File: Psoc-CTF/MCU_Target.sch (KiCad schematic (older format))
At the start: 44 parts, among them IC1 CY8C4248LQI-BL583, J4 Conn_01x04, P1 Power, P2 Analog, P3 Digital, P4 Digital, P5 CONN_01X01, P6 CONN_01X01, P7 CONN_01X01, P8 CONN_01X01, U4 FM24C04B-GTR, Y1 24MHz, Y2 32.768Khz

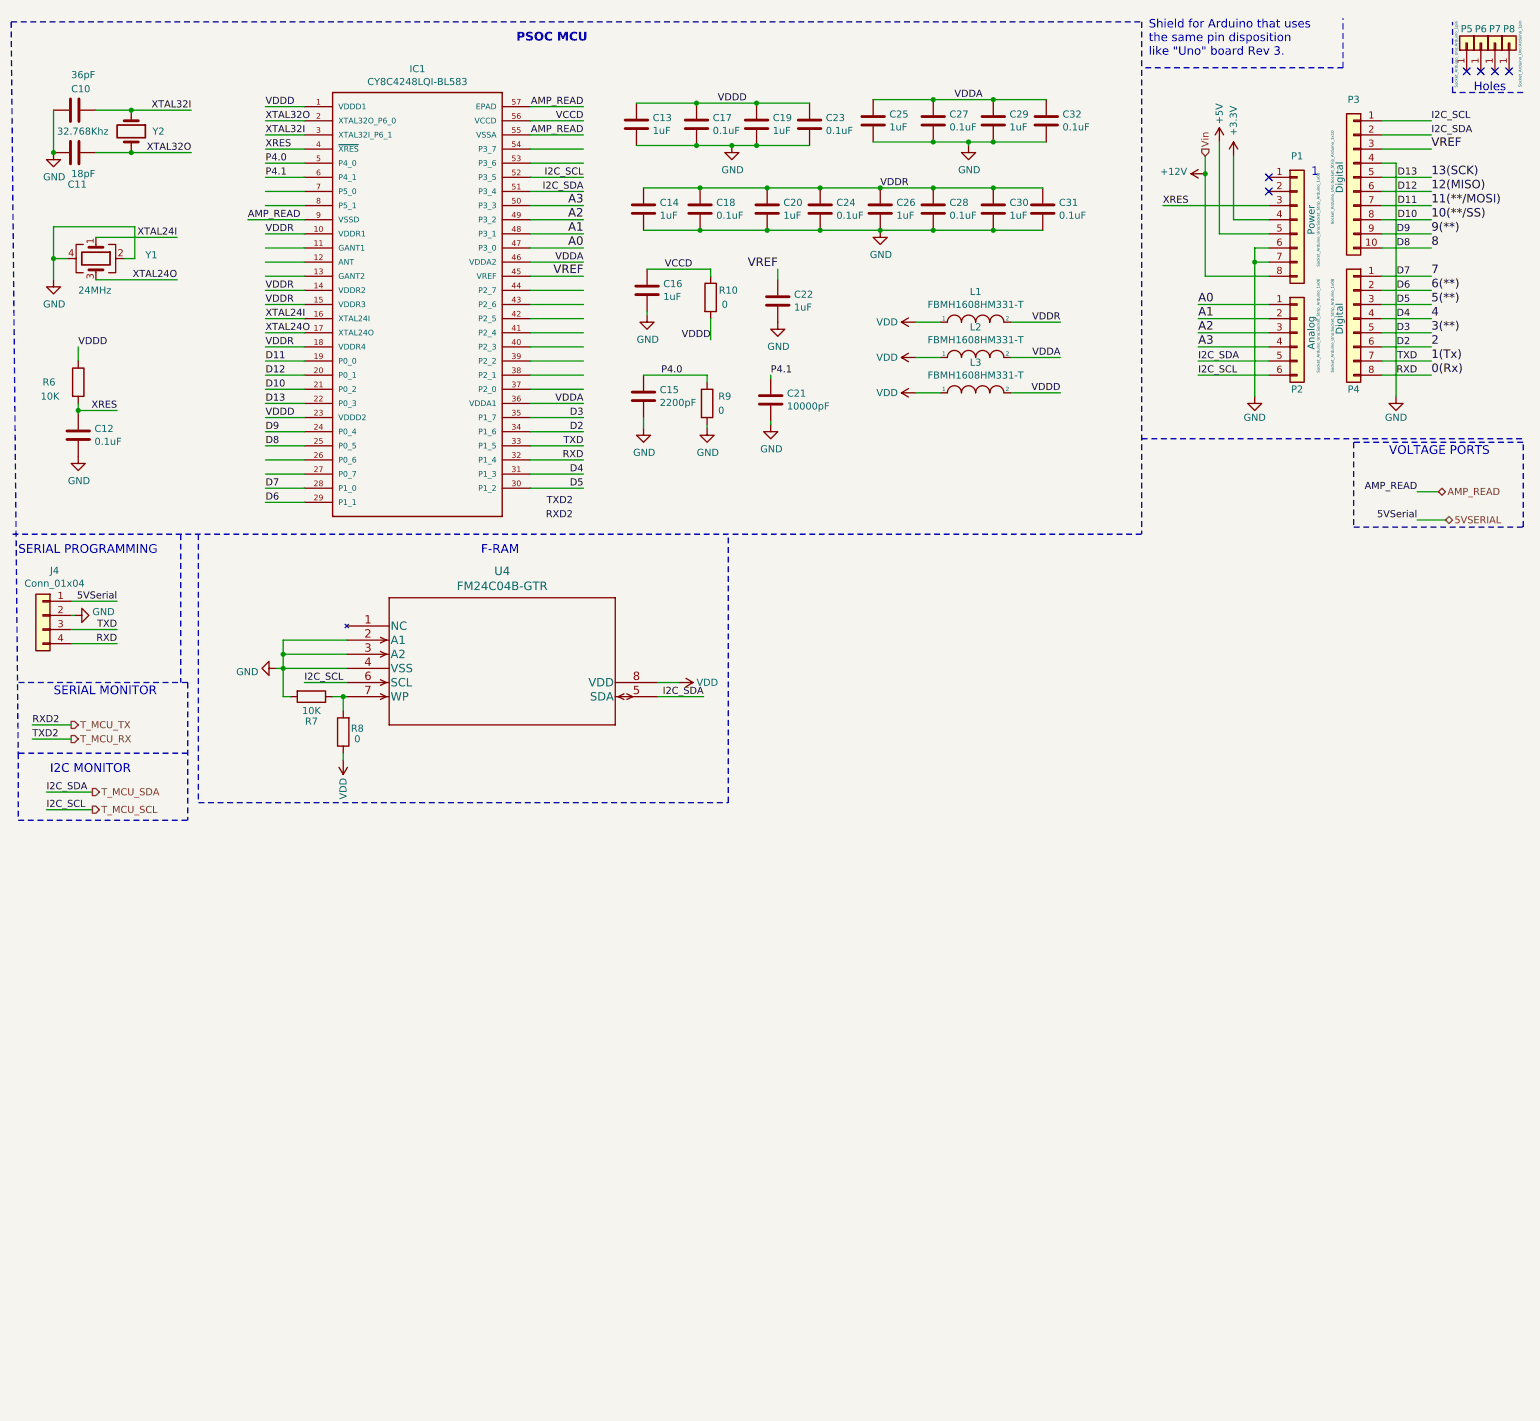
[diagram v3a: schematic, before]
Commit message: Antena agregada, pines de programación SWD
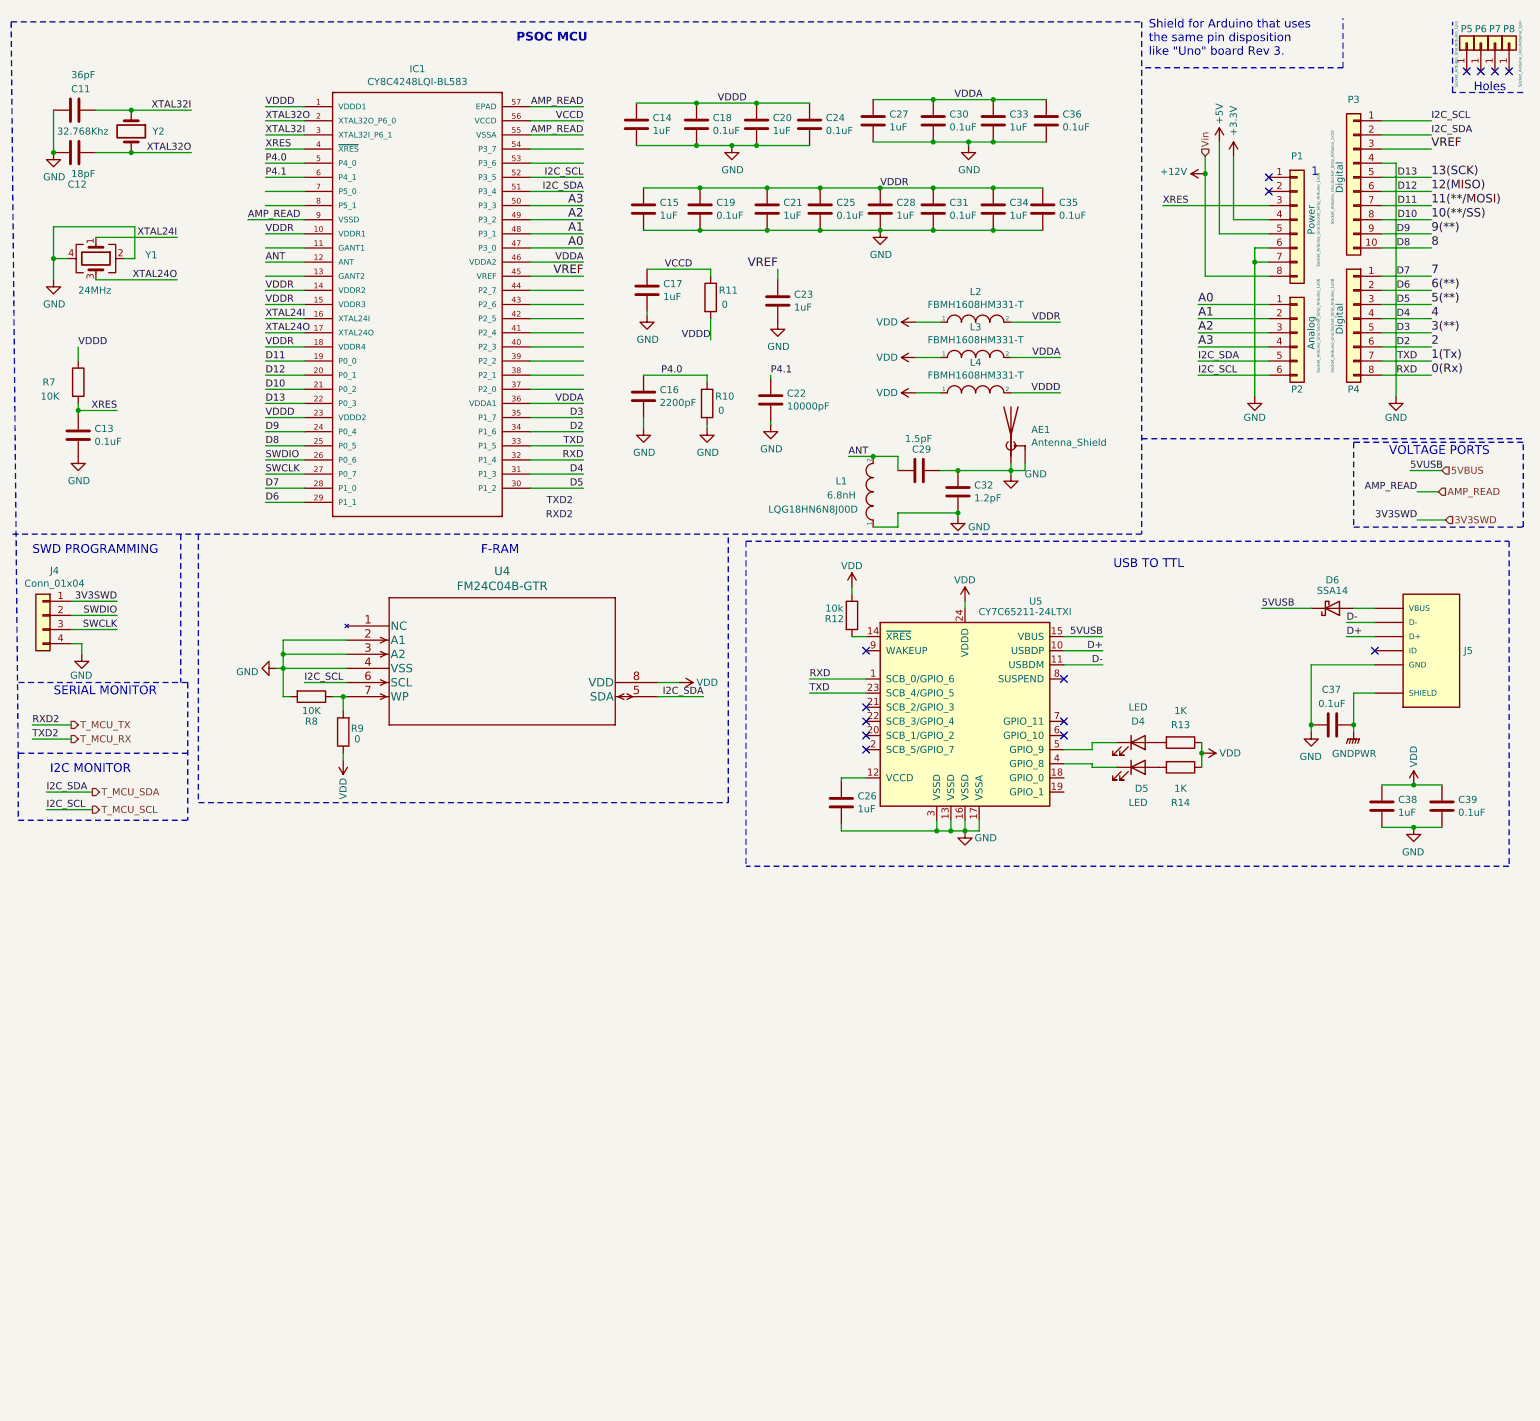
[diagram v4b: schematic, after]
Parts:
- added AE1: Antenna_Shield, symbol Device:Antenna_Shield
- added C26, C38: 1uF, Capacitor_SMD:C_0603_1608Metric_Pad1.08x0.95mm_HandSolder, symbol Device:C
- added C29: 1.5pF, Capacitor_SMD:C_0603_1608Metric_Pad1.08x0.95mm_HandSolder, symbol Device:C
- added C32: 1.2pF, Capacitor_SMD:C_0603_1608Metric_Pad1.08x0.95mm_HandSolder, symbol Device:C
- added C37, C39: 0.1uF, Capacitor_SMD:C_0603_1608Metric_Pad1.08x0.95mm_HandSolder, symbol Device:C
- added D4, D5: LED, LED_SMD:LED_0603_1608Metric_Pad1.05x0.95mm_HandSolder, symbol Device:LED
- added D6: SSA14, Diode_SMD:D_SMA_Handsoldering, symbol Device:D_Schottky
- added J5: USB3076-XX-X_REVC, Psoc-CTF:microUSB, symbol microUSB:USB3076-XX-X_REVC
- added L1: 6.8nH, Inductor_SMD:L_0603_1608Metric_Pad1.05x0.95mm_HandSolder, symbol pspice:INDUCTOR
- added R12: 10k, Resistor_SMD:R_0603_1608Metric_Pad0.98x0.95mm_HandSolder, symbol Device:R
- added R13, R14: 1K, Resistor_SMD:R_0603_1608Metric_Pad0.98x0.95mm_HandSolder, symbol Device:R
- added U5: CY7C65211-24LTXI, Package_DFN_QFN:QFN-24-1EP_4x4mm_P0.5mm_EP2.6x2.6mm, symbol Interface_USB:CY7C65211-24LTXI
- renumbered C10 to C11, C11 to C12, C12 to C13, C13 to C14, C14 to C15, C15 to C16, C16 to C17, C17 to C18, C18 to C19, C19 to C20, C20 to C21, C21 to C22, C22 to C23, C23 to C24, C24 to C25, C25 to C27, C26 to C28, C27 to C30, C28 to C31, C29 to C33, C30 to C34, C31 to C35, C32 to C36, L1 to L2, L2 to L3, L3 to L4, R9 to R10, R10 to R11, R6 to R7, R7 to R8, R8 to R9
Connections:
- net labels added: 3V3SWD, 5VBUS, 5VUSB, ANT, D+, D-, GNDPWR, SWCLK, SWDIO
- net labels removed: 5VSERIAL, 5VSerial
- wire segments 182 -> 238
- no-connect marks 6 -> 15
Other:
- note added: "SWD PROGRAMMING"
- note added: "USB TO TTL"
- note removed: "SERIAL PROGRAMMING"

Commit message: anexo slider y led rgb
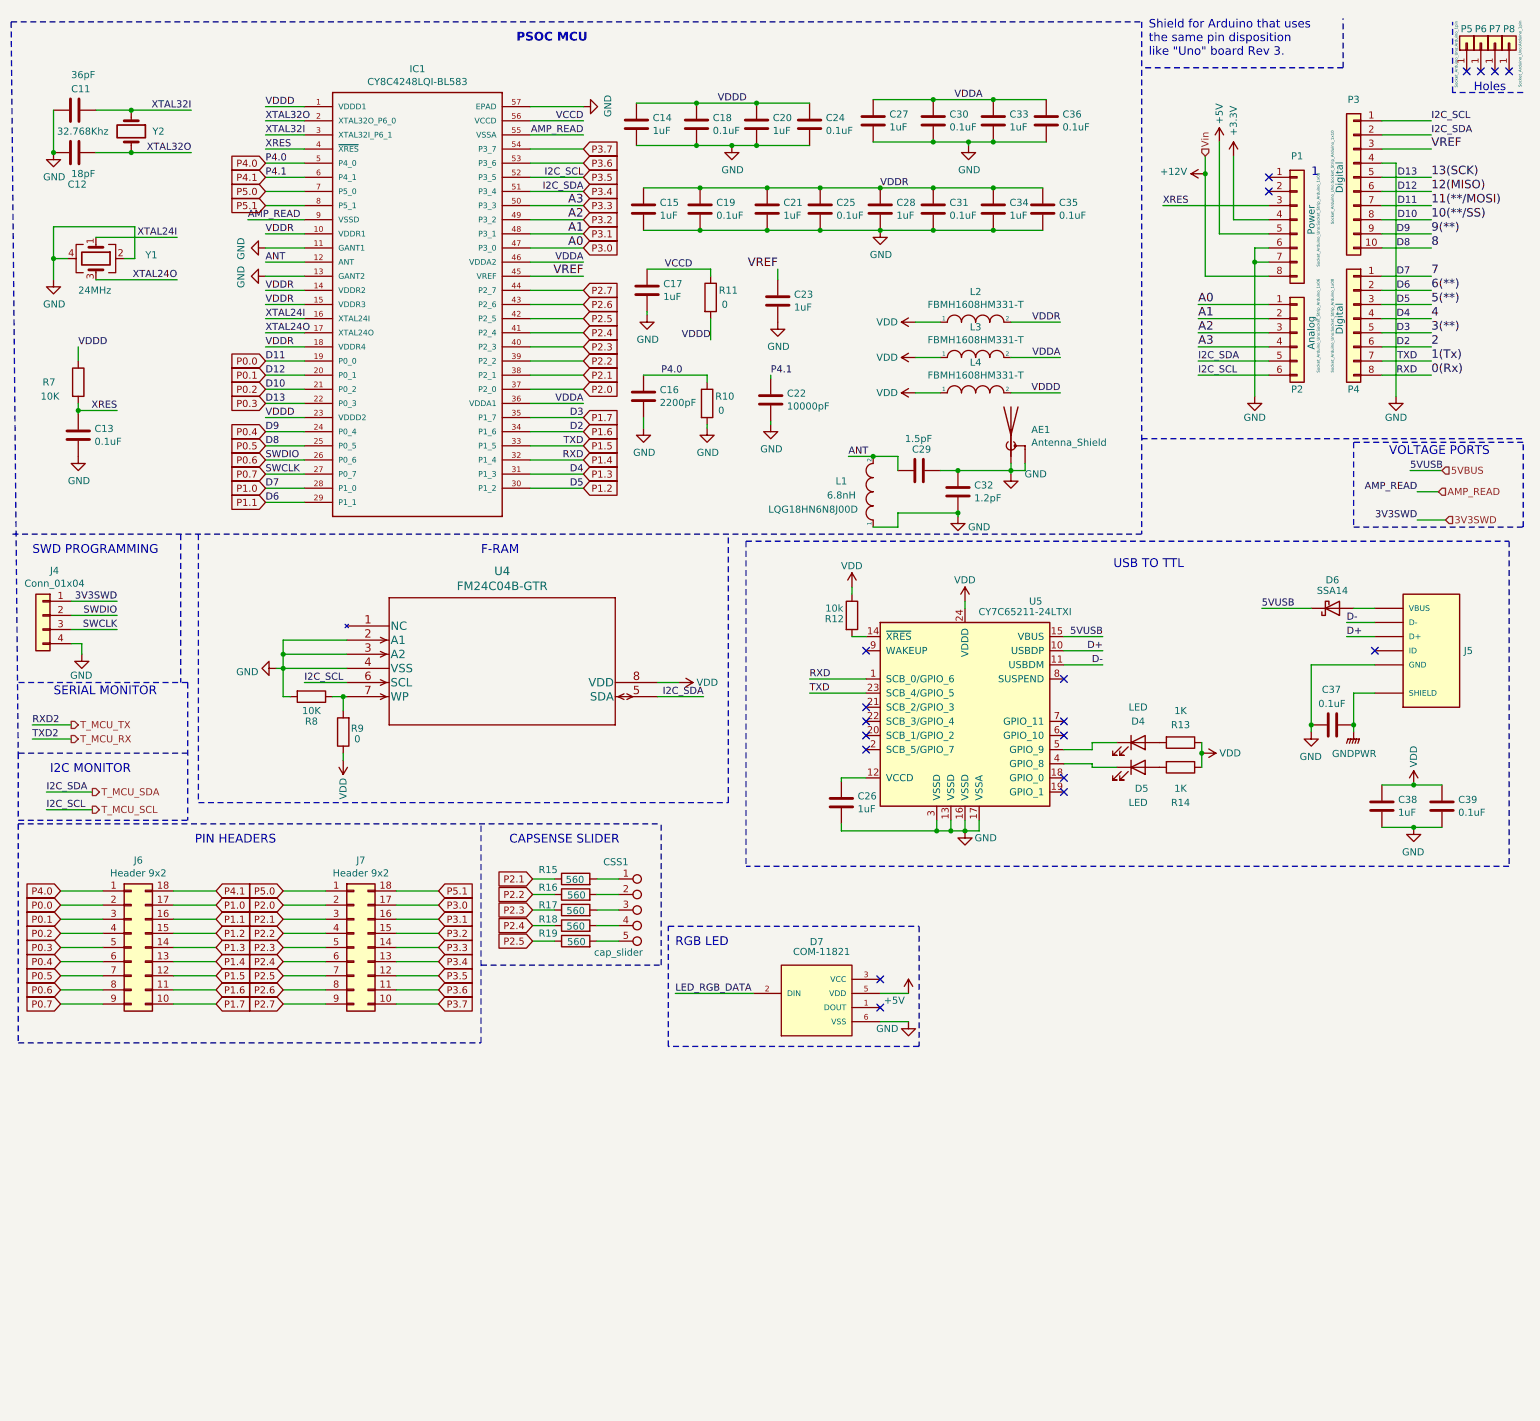
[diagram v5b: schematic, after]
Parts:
- added CSS1: cap_slider, Psoc-CTF:CAP_SLIDER_5_PADS, symbol CAP_SLIDER:cap_slider
- added D7: COM-11821, Psoc-CTF:LED_COM-11821, symbol COM-11821:COM-11821
- added J6, J7: Header 9x2, Connector_PinHeader_2.54mm:PinHeader_2x09_P2.54mm_Vertical, symbol Connector_Generic:Conn_02x09_Counter_Clockwise
- added R15, R16, R17, R18, R19: 560, Resistor_SMD:R_0603_1608Metric_Pad0.98x0.95mm_HandSolder, symbol Device:R
- AE1: footprint (none) -> Psoc-CTF:Antena_pad
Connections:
- net labels added: LED_RGB_DATA, P0.0, P0.1, P0.2, P0.3, P0.4, P0.5, P0.6, P0.7, P1.0, P1.1, P1.2, P1.3, P1.4, P1.5, P1.6, P1.7, P2.0, P2.1, P2.2, P2.3, P2.4, P2.5, P2.6, P2.7, P3.0, P3.1, P3.2, P3.3, P3.4, P3.5, P3.6, P3.7, P5.0, P5.1
- wire segments 238 -> 287
- no-connect marks 15 -> 19
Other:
- note added: "CAPSENSE SLIDER"
- note added: "PIN HEADERS"
- note added: "RGB LED"
